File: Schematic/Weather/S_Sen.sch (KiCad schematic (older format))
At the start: 27 parts, among them J4 3_Way_Wire, J5 3_Way_Wire, Q4 BSS138, Q5 AO3401, Q6 AO3401, U6 LM321

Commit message: more changes
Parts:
- renumbered C5 to C2, H8 to H10, H5 to H7, H6 to H8, H7 to H9, J4 to J11, J5 to J12, R17 to R15, R18 to R16, R19 to R17, R20 to R18, R21 to R19, R22 to R20, R23 to R21, R24 to R22, R25 to R23, R26 to R24, R27 to R25, R28 to R26, R29 to R27, R30 to R28, U6 to U5
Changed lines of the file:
@@
 $Descr A4 11693 8268
 encoding utf-8
-Sheet 10 14
+Sheet 10 15
 Title ""
 Date ""
@@
 P 5750 2350
 AR Path="/5C952539/5CA28906" Ref="U?"  Part="1"
-AR Path="/5C9F4D88/5CA28906" Ref="U6"  Part="1"
-F 0 "U6" H 5750 2831 50  0000 C CNN
+AR Path="/5C9F4D88/5CA28906" Ref="U5"  Part="1"
+F 0 "U5" H 5750 2831 50  0000 C CNN
 F 1 "LM321" H 5750 2740 50  0000 C CNN
 F 2 "Package_TO_SOT_SMD:SOT-23-5" H 5750 2350 50  0001 C CNN
@@
 P 5150 5000
 AR Path="/5C952539/5CA2890C" Ref="R?"  Part="1"
-AR Path="/5C9F4D88/5CA2890C" Ref="R17"  Part="1"
-F 0 "R17" V 4943 5000 50  0000 C CNN
+AR Path="/5C9F4D88/5CA2890C" Ref="R15"  Part="1"
+F 0 "R15" V 4943 5000 50  0000 C CNN
 F 1 "2.2K" V 5034 5000 50  0000 C CNN
 F 2 "Resistor_THT:R_Axial_DIN0204_L3.6mm_D1.6mm_P2.54mm_Vertical" V 5080 5000 50  0001 C CNN
@@
 P 5550 5450
 AR Path="/5C952539/5CA28912" Ref="R?"  Part="1"
-AR Path="/5C9F4D88/5CA28912" Ref="R20"  Part="1"
-F 0 "R20" H 5480 5404 50  0000 R CNN
+AR Path="/5C9F4D88/5CA28912" Ref="R18"  Part="1"
+F 0 "R18" H 5480 5404 50  0000 R CNN
 F 1 "5.1K" H 5480 5495 50  0000 R CNN
 F 2 "Resistor_THT:R_Axial_DIN0204_L3.6mm_D1.6mm_P2.54mm_Vertical" V 5480 5450 50  0001 C CNN
@@
 P 7050 5100
 AR Path="/5C952539/5CA28918" Ref="R?"  Part="1"
-AR Path="/5C9F4D88/5CA28918" Ref="R28"  Part="1"
-F 0 "R28" H 7120 5146 50  0000 L CNN
+AR Path="/5C9F4D88/5CA28918" Ref="R26"  Part="1"
+F 0 "R26" H 7120 5146 50  0000 L CNN
 F 1 "680" H 7120 5055 50  0000 L CNN
 F 2 "Resistor_THT:R_Axial_DIN0204_L3.6mm_D1.6mm_P2.54mm_Vertical" V 6980 5100 50  0001 C CNN
@@
 P 6750 4100
 AR Path="/5C952539/5CA2891E" Ref="R?"  Part="1"
-AR Path="/5C9F4D88/5CA2891E" Ref="R26"  Part="1"
-F 0 "R26" H 6820 4146 50  0000 L CNN
+AR Path="/5C9F4D88/5CA2891E" Ref="R24"  Part="1"
+F 0 "R24" H 6820 4146 50  0000 L CNN
 F 1 "20K" H 6820 4055 50  0000 L CNN
 F 2 "Resistor_THT:R_Axial_DIN0204_L3.6mm_D1.6mm_P2.54mm_Vertical" V 6680 4100 50  0001 C CNN
@@
 P 6000 4350
 AR Path="/5C952539/5CA28924" Ref="R?"  Part="1"
-AR Path="/5C9F4D88/5CA28924" Ref="R22"  Part="1"
-F 0 "R22" H 6070 4396 50  0000 L CNN
+AR Path="/5C9F4D88/5CA28924" Ref="R20"  Part="1"
+F 0 "R20" H 6070 4396 50  0000 L CNN
 F 1 "10K" H 6070 4305 50  0000 L CNN
 F 2 "Resistor_THT:R_Axial_DIN0204_L3.6mm_D1.6mm_P2.54mm_Vertical" V 5930 4350 50  0001 C CNN
@@
 P 5450 3900
 AR Path="/5C952539/5CA2892A" Ref="R?"  Part="1"
-AR Path="/5C9F4D88/5CA2892A" Ref="R19"  Part="1"
-F 0 "R19" H 5520 3946 50  0000 L CNN
+AR Path="/5C9F4D88/5CA2892A" Ref="R17"  Part="1"
+F 0 "R17" H 5520 3946 50  0000 L CNN
 F 1 "2.2k" H 5520 3855 50  0000 L CNN
 F 2 "Resistor_THT:R_Axial_DIN0204_L3.6mm_D1.6mm_P2.54mm_Vertical" V 5380 3900 50  0001 C CNN
@@
 P 6100 1900
 AR Path="/5C952539/5CA28930" Ref="R?"  Part="1"
-AR Path="/5C9F4D88/5CA28930" Ref="R23"  Part="1"
-F 0 "R23" H 6170 1946 50  0000 L CNN
+AR Path="/5C9F4D88/5CA28930" Ref="R21"  Part="1"
+F 0 "R21" H 6170 1946 50  0000 L CNN
 F 1 "4.7K" H 6170 1855 50  0000 L CNN
 F 2 "Resistor_THT:R_Axial_DIN0204_L3.6mm_D1.6mm_P2.54mm_Vertical" V 6030 1900 50  0001 C CNN
@@
 P 5200 2350
 AR Path="/5C952539/5CA28942" Ref="R?"  Part="1"
-AR Path="/5C9F4D88/5CA28942" Ref="R18"  Part="1"
-F 0 "R18" V 4993 2350 50  0000 C CNN
+AR Path="/5C9F4D88/5CA28942" Ref="R16"  Part="1"
+F 0 "R16" V 4993 2350 50  0000 C CNN
 F 1 "4.7K" V 5084 2350 50  0000 C CNN
 F 2 "Resistor_THT:R_Axial_DIN0204_L3.6mm_D1.6mm_P2.54mm_Vertical" V 5130 2350 50  0001 C CNN
@@
 P 6750 5100
 AR Path="/5C952539/5CA28962" Ref="R?"  Part="1"
-AR Path="/5C9F4D88/5CA28962" Ref="R27"  Part="1"
-F 0 "R27" H 6820 5146 50  0000 L CNN
+AR Path="/5C9F4D88/5CA28962" Ref="R25"  Part="1"
+F 0 "R25" H 6820 5146 50  0000 L CNN
 F 1 "20K" H 6820 5055 50  0000 L CNN
 F 2 "Resistor_THT:R_Axial_DIN0204_L3.6mm_D1.6mm_P2.54mm_Vertical" V 6680 5100 50  0001 C CNN
@@
 P 7450 2450
 AR Path="/5C952539/5CA28972" Ref="R?"  Part="1"
-AR Path="/5C9F4D88/5CA28972" Ref="R30"  Part="1"
-F 0 "R30" V 7243 2450 50  0000 C CNN
+AR Path="/5C9F4D88/5CA28972" Ref="R28"  Part="1"
+F 0 "R28" V 7243 2450 50  0000 C CNN
 F 1 "3.3k" V 7334 2450 50  0000 C CNN
 F 2 "Resistor_THT:R_Axial_DIN0204_L3.6mm_D1.6mm_P2.54mm_Vertical" V 7380 2450 50  0001 C CNN
@@
 P 6100 2850
 AR Path="/5C952539/5CA28979" Ref="R?"  Part="1"
-AR Path="/5C9F4D88/5CA28979" Ref="R24"  Part="1"
-F 0 "R24" H 6170 2896 50  0000 L CNN
+AR Path="/5C9F4D88/5CA28979" Ref="R22"  Part="1"
+F 0 "R22" H 6170 2896 50  0000 L CNN
 F 1 "4.7K" H 6170 2805 50  0000 L CNN
 F 2 "Resistor_THT:R_Axial_DIN0204_L3.6mm_D1.6mm_P2.54mm_Vertical" V 6030 2850 50  0001 C CNN
@@
 P 6600 2450
 AR Path="/5C952539/5CA28996" Ref="C?"  Part="1"
-AR Path="/5C9F4D88/5CA28996" Ref="C5"  Part="1"
-F 0 "C5" V 6348 2450 50  0000 C CNN
+AR Path="/5C9F4D88/5CA28996" Ref="C2"  Part="1"
+F 0 "C2" V 6348 2450 50  0000 C CNN
 F 1 "0.1uF" V 6439 2450 50  0000 C CNN
 F 2 "Capacitor_THT:C_Disc_D3.8mm_W2.6mm_P2.50mm" H 6638 2300 50  0001 C CNN
@@
 P 6300 2450
 AR Path="/5C952539/5CA289A0" Ref="R?"  Part="1"
-AR Path="/5C9F4D88/5CA289A0" Ref="R25"  Part="1"
-F 0 "R25" V 6093 2450 50  0000 C CNN
+AR Path="/5C9F4D88/5CA289A0" Ref="R23"  Part="1"
+F 0 "R23" V 6093 2450 50  0000 C CNN
 F 1 "4.7K" V 6184 2450 50  0000 C CNN
 F 2 "Resistor_THT:R_Axial_DIN0204_L3.6mm_D1.6mm_P2.54mm_Vertical" V 6230 2450 50  0001 C CNN
@@
 P 5600 2700
 AR Path="/5C952539/5CA289AC" Ref="R?"  Part="1"
-AR Path="/5C9F4D88/5CA289AC" Ref="R21"  Part="1"
-F 0 "R21" V 5393 2700 50  0000 C CNN
+AR Path="/5C9F4D88/5CA289AC" Ref="R19"  Part="1"
+F 0 "R19" V 5393 2700 50  0000 C CNN
 F 1 "4.7K" V 5484 2700 50  0000 C CNN
 F 2 "Resistor_THT:R_Axial_DIN0204_L3.6mm_D1.6mm_P2.54mm_Vertical" V 5530 2700 50  0001 C CNN
@@
 P 7400 4000
 AR Path="/5C952539/5CA289C7" Ref="R?"  Part="1"
-AR Path="/5C9F4D88/5CA289C7" Ref="R29"  Part="1"
-F 0 "R29" H 7470 4046 50  0000 L CNN
+AR Path="/5C9F4D88/5CA289C7" Ref="R27"  Part="1"
+F 0 "R27" H 7470 4046 50  0000 L CNN
 F 1 "47K" H 7470 3955 50  0000 L CNN
 F 2 "Resistor_THT:R_Axial_DIN0204_L3.6mm_D1.6mm_P2.54mm_Vertical" V 7330 4000 50  0001 C CNN
@@
 P 3350 2200
 AR Path="/5C952539/5CA289DB" Ref="J?"  Part="1"
-AR Path="/5C9F4D88/5CA289DB" Ref="J5"  Part="1"
-F 0 "J5" H 3200 1800 50  0000 L CNN
+AR Path="/5C9F4D88/5CA289DB" Ref="J12"  Part="1"
+F 0 "J12" H 3200 1800 50  0000 L CNN
 F 1 "3_Way_Wire" H 3150 1650 50  0000 L CNN
 F 2 "Connector_PinHeader_2.54mm:PinHeader_1x03_P2.54mm_Vertical" H 3350 2200 50  0001 C CNN
@@
 P 3300 3550
 AR Path="/5C952539/5CA289E6" Ref="J?"  Part="1"
-AR Path="/5C9F4D88/5CA289E6" Ref="J4"  Part="1"
-F 0 "J4" H 3200 3150 50  0000 L CNN
+AR Path="/5C9F4D88/5CA289E6" Ref="J11"  Part="1"
+F 0 "J11" H 3200 3150 50  0000 L CNN
 F 1 "3_Way_Wire" H 3150 3000 50  0000 L CNN
 F 2 "Connector_PinHeader_2.54mm:PinHeader_1x03_P2.54mm_Vertical" H 3300 3550 50  0001 C CNN
@@
 Connection ~ 5450 3650
 $Comp
-L Mechanical:MountingHole_Pad H5
+L Mechanical:MountingHole_Pad H7
 U 1 1 5CA2EA1E
 P 8050 3550
-F 0 "H5" H 8150 3599 50  0000 L CNN
+F 0 "H7" H 8150 3599 50  0000 L CNN
 F 1 "MountingHole_Pad" H 8150 3508 50  0000 L CNN
 F 2 "Connector_Wire:SolderWirePad_1x01_Drill0.8mm" H 8050 3550 50  0001 C CNN
@@
 $EndComp
 $Comp
-L Mechanical:MountingHole_Pad H7
+L Mechanical:MountingHole_Pad H9
 U 1 1 5CA3B689
 P 8050 4050
-F 0 "H7" H 8150 4099 50  0000 L CNN
+F 0 "H9" H 8150 4099 50  0000 L CNN
 F 1 "MountingHole_Pad" H 8150 4008 50  0000 L CNN
 F 2 "Connector_Wire:SolderWirePad_1x01_Drill0.8mm" H 8050 4050 50  0001 C CNN
@@
 $EndComp
 $Comp
-L Mechanical:MountingHole_Pad H6
+L Mechanical:MountingHole_Pad H8
 U 1 1 5CA554AA
 P 8050 3750
-F 0 "H6" H 7950 3707 50  0000 R CNN
+F 0 "H8" H 7950 3707 50  0000 R CNN
 F 1 "MountingHole_Pad" H 7950 3798 50  0000 R CNN
 F 2 "Connector_Wire:SolderWirePad_1x01_Drill0.8mm" H 8050 3750 50  0001 C CNN
@@
 $EndComp
 $Comp
-L Mechanical:MountingHole_Pad H8
+L Mechanical:MountingHole_Pad H10
 U 1 1 5CA56382
 P 8050 4250
-F 0 "H8" H 7950 4207 50  0000 R CNN
+F 0 "H10" H 7950 4207 50  0000 R CNN
 F 1 "MountingHole_Pad" H 7950 4298 50  0000 R CNN
 F 2 "Connector_Wire:SolderWirePad_1x01_Drill0.8mm" H 8050 4250 50  0001 C CNN

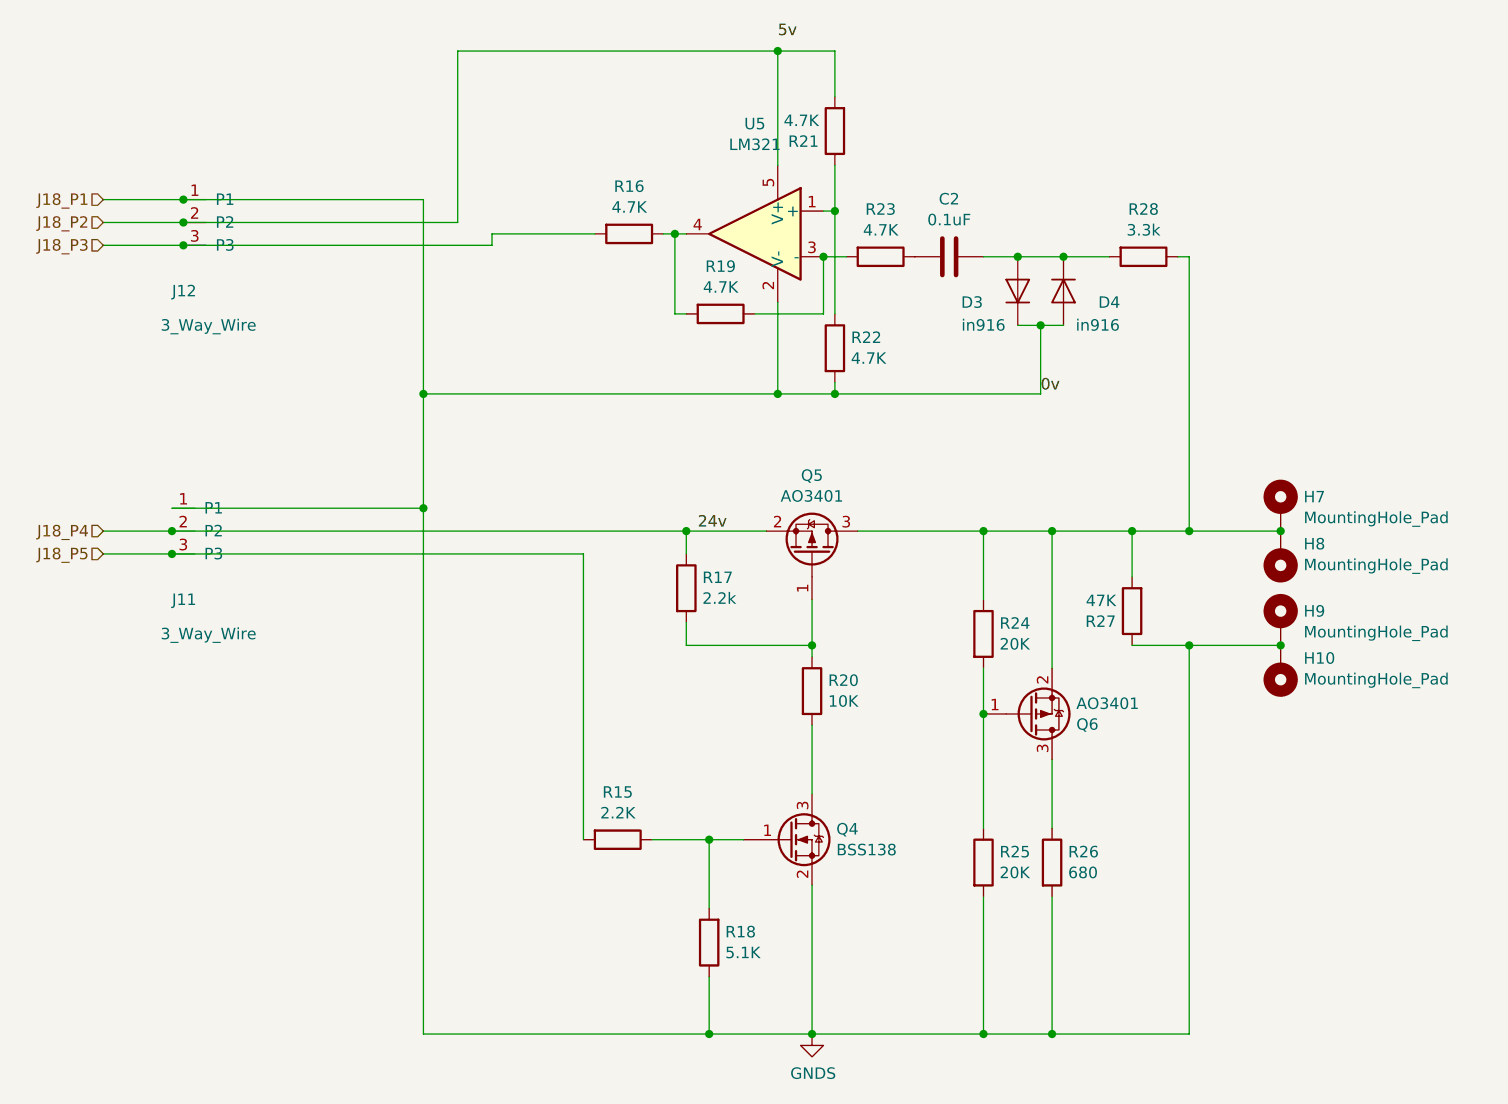
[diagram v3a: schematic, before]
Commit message: Connector relable start
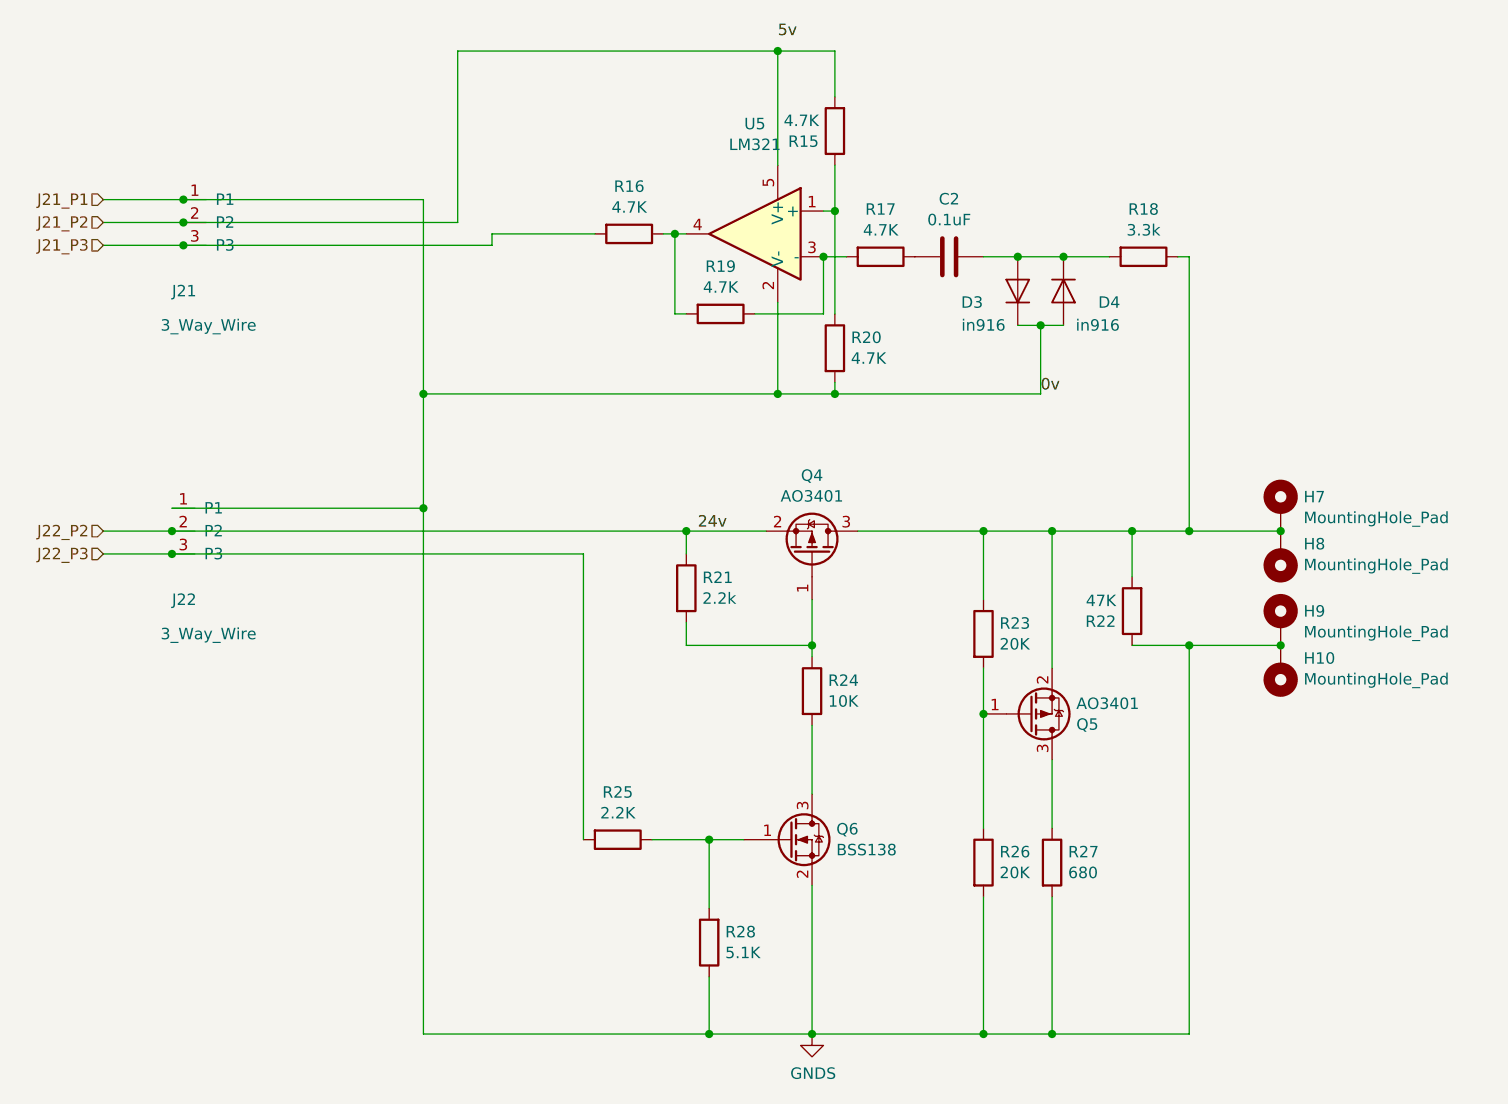
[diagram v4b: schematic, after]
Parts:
- renumbered J12 to J21, J11 to J22, Q5 to Q4, Q6 to Q5, Q4 to Q6, R21 to R15, R23 to R17, R28 to R18, R22 to R20, R17 to R21, R27 to R22, R24 to R23, R20 to R24, R15 to R25, R25 to R26, R26 to R27, R18 to R28
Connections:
- net J18_P2 renamed J21_P2
- net J18_P3 renamed J21_P3
- net J18_P4 renamed J22_P2
- net J18_P5 renamed J22_P3
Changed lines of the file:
@@
 $Descr A4 11693 8268
 encoding utf-8
-Sheet 10 15
+Sheet 8 15
 Title ""
 Date ""
@@
 $EndDescr
 Text HLabel 2900 2200 0    50   Input ~ 0
-J18_P1
+J21_P1
 Text HLabel 2900 2300 0    50   Input ~ 0
-J18_P2
+J21_P2
 Text HLabel 2900 2400 0    50   Input ~ 0
-J18_P3
+J21_P3
 Text HLabel 2900 3650 0    50   Input ~ 0
-J18_P4
+J22_P2
 $Comp
 L Weather-rescue:AO3401-Transistor_FET Q?
@@
 P 6000 3750
 AR Path="/5C952539/5CA288FA" Ref="Q?"  Part="1"
-AR Path="/5C9F4D88/5CA288FA" Ref="Q5"  Part="1"
-F 0 "Q5" V 6343 3750 50  0000 C CNN
+AR Path="/5C9F4D88/5CA288FA" Ref="Q4"  Part="1"
+F 0 "Q4" V 6343 3750 50  0000 C CNN
 F 1 "AO3401" V 6252 3750 50  0000 C CNN
 F 2 "Package_TO_SOT_SMD:SOT-23" H 6200 3675 50  0001 L CIN
@@
 P 5900 5000
 AR Path="/5C952539/5CA28900" Ref="Q?"  Part="1"
-AR Path="/5C9F4D88/5CA28900" Ref="Q4"  Part="1"
-F 0 "Q4" H 6106 5046 50  0000 L CNN
+AR Path="/5C9F4D88/5CA28900" Ref="Q6"  Part="1"
+F 0 "Q6" H 6106 5046 50  0000 L CNN
 F 1 "BSS138" H 6106 4955 50  0000 L CNN
 F 2 "Package_TO_SOT_SMD:SOT-23" H 6100 4925 50  0001 L CIN
@@
 P 5150 5000
 AR Path="/5C952539/5CA2890C" Ref="R?"  Part="1"
-AR Path="/5C9F4D88/5CA2890C" Ref="R15"  Part="1"
-F 0 "R15" V 4943 5000 50  0000 C CNN
+AR Path="/5C9F4D88/5CA2890C" Ref="R25"  Part="1"
+F 0 "R25" V 4943 5000 50  0000 C CNN
 F 1 "2.2K" V 5034 5000 50  0000 C CNN
 F 2 "Resistor_THT:R_Axial_DIN0204_L3.6mm_D1.6mm_P2.54mm_Vertical" V 5080 5000 50  0001 C CNN
@@
 P 5550 5450
 AR Path="/5C952539/5CA28912" Ref="R?"  Part="1"
-AR Path="/5C9F4D88/5CA28912" Ref="R18"  Part="1"
-F 0 "R18" H 5480 5404 50  0000 R CNN
+AR Path="/5C9F4D88/5CA28912" Ref="R28"  Part="1"
+F 0 "R28" H 5480 5404 50  0000 R CNN
 F 1 "5.1K" H 5480 5495 50  0000 R CNN
 F 2 "Resistor_THT:R_Axial_DIN0204_L3.6mm_D1.6mm_P2.54mm_Vertical" V 5480 5450 50  0001 C CNN
@@
 P 7050 5100
 AR Path="/5C952539/5CA28918" Ref="R?"  Part="1"
-AR Path="/5C9F4D88/5CA28918" Ref="R26"  Part="1"
-F 0 "R26" H 7120 5146 50  0000 L CNN
+AR Path="/5C9F4D88/5CA28918" Ref="R27"  Part="1"
+F 0 "R27" H 7120 5146 50  0000 L CNN
 F 1 "680" H 7120 5055 50  0000 L CNN
 F 2 "Resistor_THT:R_Axial_DIN0204_L3.6mm_D1.6mm_P2.54mm_Vertical" V 6980 5100 50  0001 C CNN
@@
 P 6750 4100
 AR Path="/5C952539/5CA2891E" Ref="R?"  Part="1"
-AR Path="/5C9F4D88/5CA2891E" Ref="R24"  Part="1"
-F 0 "R24" H 6820 4146 50  0000 L CNN
+AR Path="/5C9F4D88/5CA2891E" Ref="R23"  Part="1"
+F 0 "R23" H 6820 4146 50  0000 L CNN
 F 1 "20K" H 6820 4055 50  0000 L CNN
 F 2 "Resistor_THT:R_Axial_DIN0204_L3.6mm_D1.6mm_P2.54mm_Vertical" V 6680 4100 50  0001 C CNN
@@
 P 6000 4350
 AR Path="/5C952539/5CA28924" Ref="R?"  Part="1"
-AR Path="/5C9F4D88/5CA28924" Ref="R20"  Part="1"
-F 0 "R20" H 6070 4396 50  0000 L CNN
+AR Path="/5C9F4D88/5CA28924" Ref="R24"  Part="1"
+F 0 "R24" H 6070 4396 50  0000 L CNN
 F 1 "10K" H 6070 4305 50  0000 L CNN
 F 2 "Resistor_THT:R_Axial_DIN0204_L3.6mm_D1.6mm_P2.54mm_Vertical" V 5930 4350 50  0001 C CNN
@@
 P 5450 3900
 AR Path="/5C952539/5CA2892A" Ref="R?"  Part="1"
-AR Path="/5C9F4D88/5CA2892A" Ref="R17"  Part="1"
-F 0 "R17" H 5520 3946 50  0000 L CNN
+AR Path="/5C9F4D88/5CA2892A" Ref="R21"  Part="1"
+F 0 "R21" H 5520 3946 50  0000 L CNN
 F 1 "2.2k" H 5520 3855 50  0000 L CNN
 F 2 "Resistor_THT:R_Axial_DIN0204_L3.6mm_D1.6mm_P2.54mm_Vertical" V 5380 3900 50  0001 C CNN
@@
 P 6100 1900
 AR Path="/5C952539/5CA28930" Ref="R?"  Part="1"
-AR Path="/5C9F4D88/5CA28930" Ref="R21"  Part="1"
-F 0 "R21" H 6170 1946 50  0000 L CNN
+AR Path="/5C9F4D88/5CA28930" Ref="R15"  Part="1"
+F 0 "R15" H 6170 1946 50  0000 L CNN
 F 1 "4.7K" H 6170 1855 50  0000 L CNN
 F 2 "Resistor_THT:R_Axial_DIN0204_L3.6mm_D1.6mm_P2.54mm_Vertical" V 6030 1900 50  0001 C CNN
@@
 P 6950 4450
 AR Path="/5C952539/5CA2895B" Ref="Q?"  Part="1"
-AR Path="/5C9F4D88/5CA2895B" Ref="Q6"  Part="1"
-F 0 "Q6" H 7156 4496 50  0000 L CNN
+AR Path="/5C9F4D88/5CA2895B" Ref="Q5"  Part="1"
+F 0 "Q5" H 7156 4496 50  0000 L CNN
 F 1 "AO3401" H 7156 4405 50  0000 L CNN
 F 2 "Package_TO_SOT_SMD:SOT-23" H 7150 4375 50  0001 L CIN
@@
 P 6750 5100
 AR Path="/5C952539/5CA28962" Ref="R?"  Part="1"
-AR Path="/5C9F4D88/5CA28962" Ref="R25"  Part="1"
-F 0 "R25" H 6820 5146 50  0000 L CNN
+AR Path="/5C9F4D88/5CA28962" Ref="R26"  Part="1"
+F 0 "R26" H 6820 5146 50  0000 L CNN
 F 1 "20K" H 6820 5055 50  0000 L CNN
 F 2 "Resistor_THT:R_Axial_DIN0204_L3.6mm_D1.6mm_P2.54mm_Vertical" V 6680 5100 50  0001 C CNN
@@
 P 7450 2450
 AR Path="/5C952539/5CA28972" Ref="R?"  Part="1"
-AR Path="/5C9F4D88/5CA28972" Ref="R28"  Part="1"
-F 0 "R28" V 7243 2450 50  0000 C CNN
+AR Path="/5C9F4D88/5CA28972" Ref="R18"  Part="1"
+F 0 "R18" V 7243 2450 50  0000 C CNN
 F 1 "3.3k" V 7334 2450 50  0000 C CNN
 F 2 "Resistor_THT:R_Axial_DIN0204_L3.6mm_D1.6mm_P2.54mm_Vertical" V 7380 2450 50  0001 C CNN
@@
 P 6100 2850
 AR Path="/5C952539/5CA28979" Ref="R?"  Part="1"
-AR Path="/5C9F4D88/5CA28979" Ref="R22"  Part="1"
-F 0 "R22" H 6170 2896 50  0000 L CNN
+AR Path="/5C9F4D88/5CA28979" Ref="R20"  Part="1"
+F 0 "R20" H 6170 2896 50  0000 L CNN
 F 1 "4.7K" H 6170 2805 50  0000 L CNN
 F 2 "Resistor_THT:R_Axial_DIN0204_L3.6mm_D1.6mm_P2.54mm_Vertical" V 6030 2850 50  0001 C CNN
@@
 P 6300 2450
 AR Path="/5C952539/5CA289A0" Ref="R?"  Part="1"
-AR Path="/5C9F4D88/5CA289A0" Ref="R23"  Part="1"
-F 0 "R23" V 6093 2450 50  0000 C CNN
+AR Path="/5C9F4D88/5CA289A0" Ref="R17"  Part="1"
+F 0 "R17" V 6093 2450 50  0000 C CNN
 F 1 "4.7K" V 6184 2450 50  0000 C CNN
 F 2 "Resistor_THT:R_Axial_DIN0204_L3.6mm_D1.6mm_P2.54mm_Vertical" V 6230 2450 50  0001 C CNN
@@
 Connection ~ 6050 2450
 Text HLabel 2900 3750 0    50   Input ~ 0
-J18_P5
+J22_P3
 Wire Wire Line
 	5450 4050 5450 4150
@@
 P 7400 4000
 AR Path="/5C952539/5CA289C7" Ref="R?"  Part="1"
-AR Path="/5C9F4D88/5CA289C7" Ref="R27"  Part="1"
-F 0 "R27" H 7470 4046 50  0000 L CNN
+AR Path="/5C9F4D88/5CA289C7" Ref="R22"  Part="1"
+F 0 "R22" H 7470 4046 50  0000 L CNN
 F 1 "47K" H 7470 3955 50  0000 L CNN
 F 2 "Resistor_THT:R_Axial_DIN0204_L3.6mm_D1.6mm_P2.54mm_Vertical" V 7330 4000 50  0001 C CNN
@@
 P 3350 2200
 AR Path="/5C952539/5CA289DB" Ref="J?"  Part="1"
-AR Path="/5C9F4D88/5CA289DB" Ref="J12"  Part="1"
-F 0 "J12" H 3200 1800 50  0000 L CNN
+AR Path="/5C9F4D88/5CA289DB" Ref="J21"  Part="1"
+F 0 "J21" H 3200 1800 50  0000 L CNN
 F 1 "3_Way_Wire" H 3150 1650 50  0000 L CNN
 F 2 "Connector_PinHeader_2.54mm:PinHeader_1x03_P2.54mm_Vertical" H 3350 2200 50  0001 C CNN
@@
 P 3300 3550
 AR Path="/5C952539/5CA289E6" Ref="J?"  Part="1"
-AR Path="/5C9F4D88/5CA289E6" Ref="J11"  Part="1"
-F 0 "J11" H 3200 3150 50  0000 L CNN
+AR Path="/5C9F4D88/5CA289E6" Ref="J22"  Part="1"
+F 0 "J22" H 3200 3150 50  0000 L CNN
 F 1 "3_Way_Wire" H 3150 3000 50  0000 L CNN
 F 2 "Connector_PinHeader_2.54mm:PinHeader_1x03_P2.54mm_Vertical" H 3300 3550 50  0001 C CNN
